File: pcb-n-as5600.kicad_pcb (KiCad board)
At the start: 2 copper layers, 31 x 31 mm, 31 parts, among them J1 Conn_01x04_Pin, J2 Conn_01x04_Pin, J3 Conn_01x04_Pin, J6 USB_C_Receptacle_USB2.0_14P, U1 AMS1117, U4 AS5600, U5 STM32F103C8Tx, Y2 8MHz

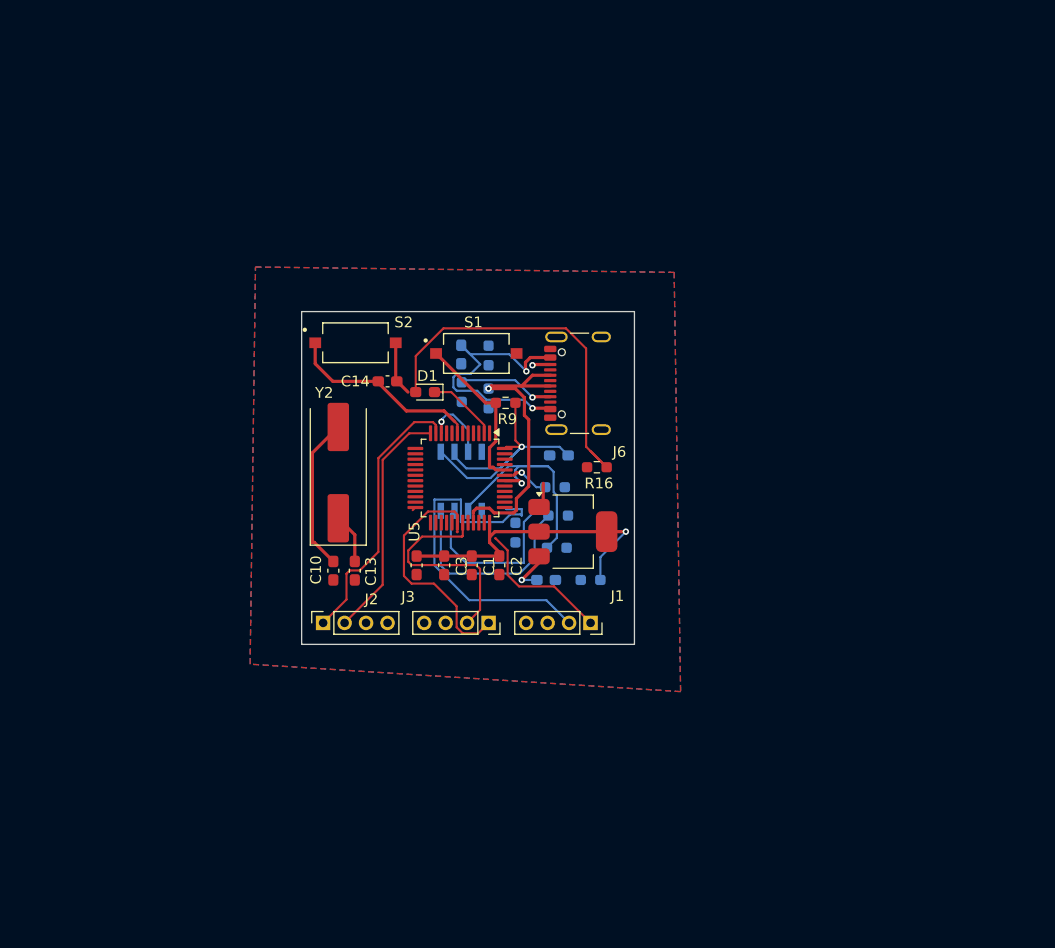
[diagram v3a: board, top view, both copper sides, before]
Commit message: addition of mount holes
rechecked voltage connections as well, and added
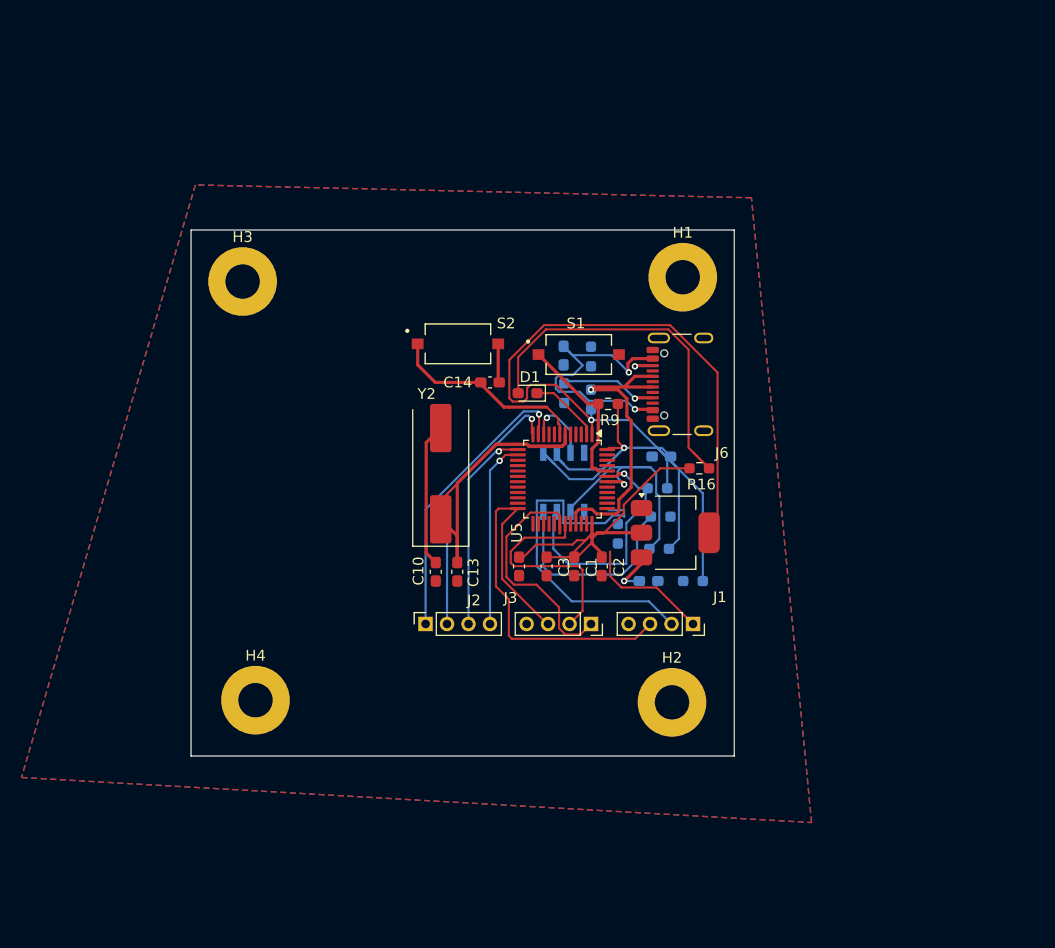
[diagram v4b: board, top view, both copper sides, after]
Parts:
- added H1: MountingHole, MountingHole:MountingHole_3.2mm_M3_Pad, F.Cu at (157.0, 53.8)
- added H2: MountingHole, MountingHole:MountingHole_3.2mm_M3_Pad, F.Cu at (156.0, 93.4)
- added H3: MountingHole, MountingHole:MountingHole_3.2mm_M3_Pad, F.Cu at (116.0, 54.2)
- added H4: MountingHole, MountingHole:MountingHole_3.2mm_M3_Pad, F.Cu at (117.2, 93.2)
- moved C11 9.54 mm to (141.8, 80.7)
- moved C2 9.54 mm to (149.5, 80.7)
- moved J1 9.54 mm to (158.0, 86.1)
- moved J3 9.54 mm to (148.5, 86.1)
- moved R11 9.54 mm to (146.0, 64.6)
- moved R13 9.54 mm to (154.6, 73.5)
- moved R2 9.54 mm to (148.5, 65.2)
- moved R3 9.54 mm to (151.0, 77.7)
- moved R4 9.54 mm to (158.0, 82.1)
- moved R7 9.54 mm to (154.8, 79.1)
- moved R8 9.54 mm to (148.5, 61.2)
- moved U1 9.54 mm to (156.3, 77.6)
- moved Y2 9.54 mm to (134.5, 72.1)
- moved C10 9.54 mm to (134.0, 81.2)
- moved C13 9.54 mm to (136.0, 81.2)
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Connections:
- J1 pad 3: /3.3V -> +3.3V
- J3 pad 3: /3.3V -> +3.3V
- R13 pad 1: /3.3V -> +3.3V
- R16 pad 2: /3.3V -> +3.3V
- R2 pad 1: /3.3V -> +3.3V
- R7 pad 1: /3.3V -> +3.3V
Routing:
- net +3.3V: track 58.3 -> 201.3 mm
- net /OSC_OUT: track 4.66 -> 41.2 mm
- net dum3: track 0.00 -> 19.3 mm, vias 0 -> 1
- net dum4: track 0.00 -> 17.5 mm, vias 0 -> 1
- net dum2: track 22.1 -> 24.6 mm, vias 0 -> 1
- net Net-(U1-ADJ): track 2.36 -> 0.55 mm
- net SWDIO: track 13.5 -> 11.9 mm
- net GND: track 5.07 -> 3.46 mm
- net dum1: track 25.7 -> 27.1 mm, vias 0 -> 1
- net /OSC_IN: track 14.4 -> 13.5 mm
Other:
- board size 31 x 31 mm -> 50.6 x 49 mm

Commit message: final pcb with proper connections
removed UART due to lack of use, connections are correct, slight silk screen issue, final draft
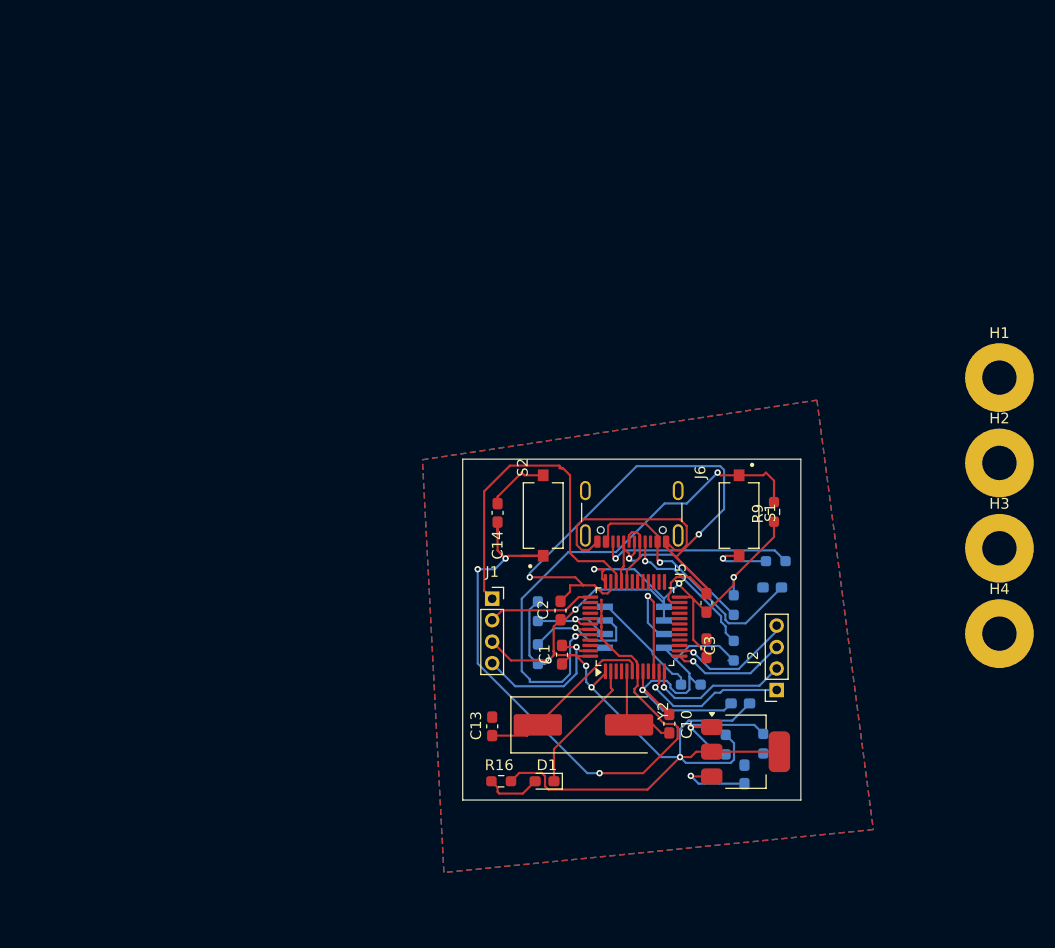
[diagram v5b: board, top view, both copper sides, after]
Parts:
- removed J3: Conn_01x04_Pin, Connector_PinSocket_2.00mm:PinSocket_1x04_P2.00mm_Vertical
- moved H3 74.8 mm to (186.5, 79.0)
- moved H4 69.6 mm to (186.5, 87.0)
- moved H2 37.8 mm to (186.5, 71.1)
- moved D1 36.2 mm to (144.1, 100.8)
- moved R16 34.5 mm to (140.1, 100.8), turned to 0 degrees
- moved J2 33.3 mm to (165.8, 92.2), turned to 180 degrees
- moved H1 30.9 mm to (186.5, 63.1)
- moved C8 29.1 mm to (165.3, 82.7), turned to 0 degrees
- moved R11 28.7 mm to (161.8, 88.6)
- moved Y2 26.9 mm to (147.8, 95.5), turned to 0 degrees
- moved C10 26.0 mm to (155.8, 95.4), turned to -90 degrees
- moved R8 25.7 mm to (165.7, 80.2), turned to 0 degrees
- moved C7 24.1 mm to (162.4, 93.5)
- moved R3 23.8 mm to (164.5, 97.2)
- moved R2 23.3 mm to (161.8, 84.3), turned to -90 degrees
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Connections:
- U5 pad 30: /TX -> unconnected-(U5-PA9-Pad30)
- U5 pad 31: /RX -> unconnected-(U5-PA10-Pad31)
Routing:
- net GND: track 3.46 -> 136.9 mm, vias 0 -> 5
- net +3.3V: track 201.3 -> 134.7 mm, vias 2 -> 8
- net NRST: track 18.7 -> 63.7 mm, vias 0 -> 3
- net BOOTO: track 14.4 -> 48.2 mm, vias 0 -> 2
- net Net-(D1-A): track 35.1 -> 5.28 mm
- net /OSC_OUT: track 41.2 -> 16.8 mm
- net SCLK: track 33.7 -> 10.0 mm
- net /TX: track 22.2 -> 0.00 mm
- net SWDIO: track 11.9 -> 33.0 mm
- net /RX: track 20.4 -> 0.00 mm
- net Net-(J6-CC2): track 1.69 -> 18.2 mm
- net SDA: track 24.1 -> 8.47 mm
- net Net-(U1-ADJ): track 0.55 -> 13.5 mm, vias 0 -> 1
- net dum1: track 27.1 -> 14.8 mm
- net dum2: track 24.6 -> 13.6 mm
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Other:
- board size 50.6 x 49 mm -> 31.5 x 31.8 mm

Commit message: final with mounting
changed shape of PCB to accomadate mounting holes
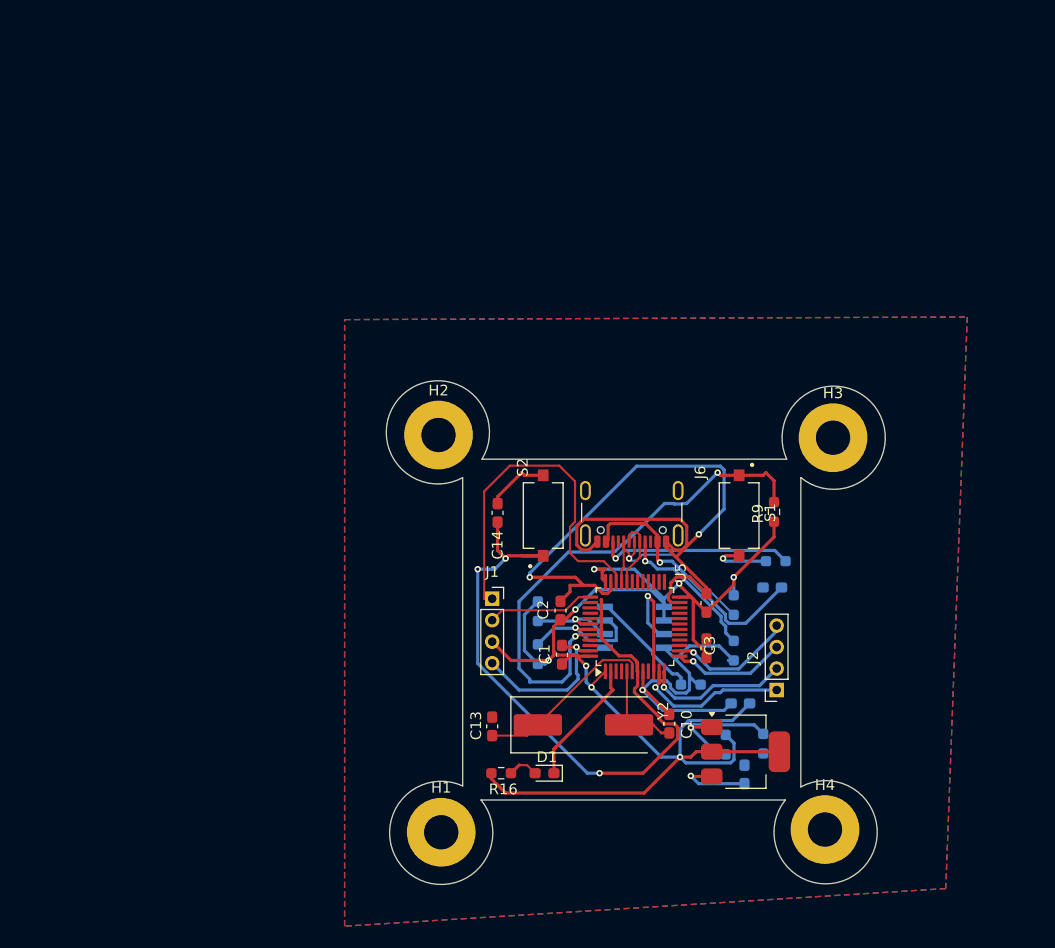
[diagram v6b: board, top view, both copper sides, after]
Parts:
- moved H1 67.1 mm to (134.5, 105.5)
- moved H2 52.3 mm to (134.2, 68.5)
- moved H4 24.4 mm to (170.2, 105.2)
- moved H3 18.6 mm to (171.0, 68.8)
- moved D1 0.75 mm to (144.1, 100.0)
- moved R16 0.75 mm to (140.1, 100.0), turned to 180 degrees
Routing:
- net Net-(D1-A): track 5.28 -> 2.89 mm
- net +3.3V: track 134.7 -> 136.6 mm
- net GND: track 136.9 -> 137.7 mm
- net SWDIO: track 33.0 -> 33.6 mm
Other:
- board size 31.5 x 31.8 mm -> 46.5 x 46.9 mm

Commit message: final changes
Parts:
- moved R2 1.18 mm to (161.8, 83.2)
- moved S2 0.90 mm to (143.2, 76.5)
- moved C14 0.75 mm to (139.0, 75.8)
- moved C4 0.37 mm to (163.0, 100.4)
- moved C10 0.25 mm to (155.8, 95.6)
- moved H2 0.25 mm to (134.2, 68.2)
- moved R1 0.25 mm to (157.8, 91.5)
- turned C3 to -90 degrees
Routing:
- net GND: track 137.7 -> 120.5 mm, vias 5 -> 7
- net NRST: track 63.7 -> 50.1 mm, vias 3 -> 2
- net /OSC_IN: track 9.13 -> 18.3 mm, vias 0 -> 2
- net SCL: track 12.4 -> 17.9 mm
- net SWDIO: track 33.6 -> 36.8 mm
- net dum2: track 13.6 -> 14.8 mm
- net Net-(J6-CC1): track 13.8 -> 14.7 mm
- net Net-(U4-DIR): track 10.6 -> 11.4 mm
- net Net-(C8-Pad2): track 24.8 -> 24.1 mm
- net dum4: track 11.7 -> 12.4 mm
- net +3.3V: track 136.6 -> 137.3 mm
- net dum3: track 10.7 -> 11.3 mm
- net +5V: track 7.27 -> 7.79 mm
- net MCU_D+: track 19.8 -> 19.3 mm

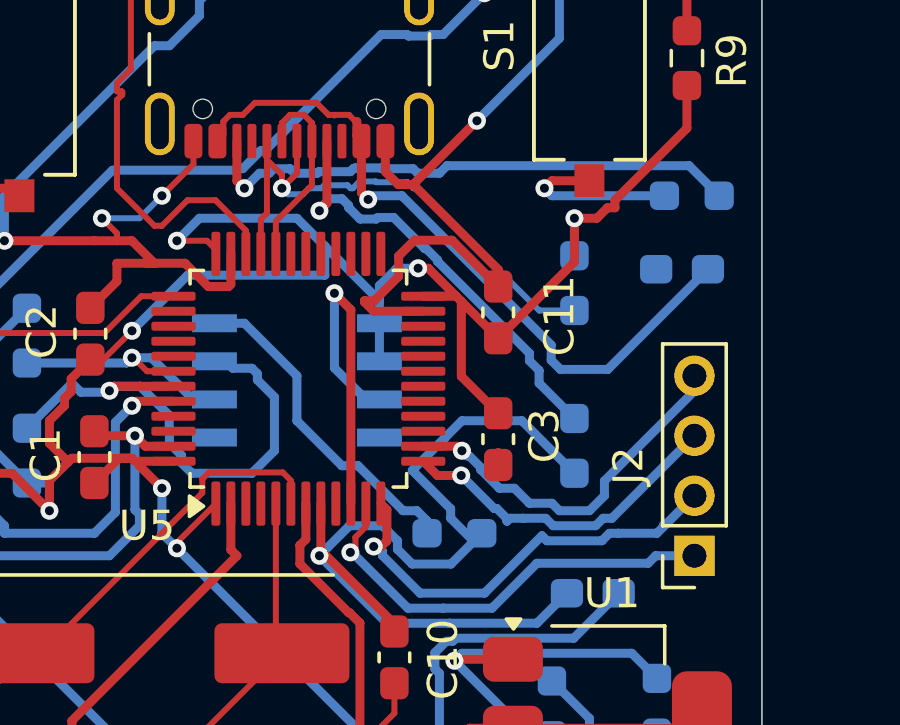
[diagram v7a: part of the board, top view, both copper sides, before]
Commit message: changed switch and updated BOM
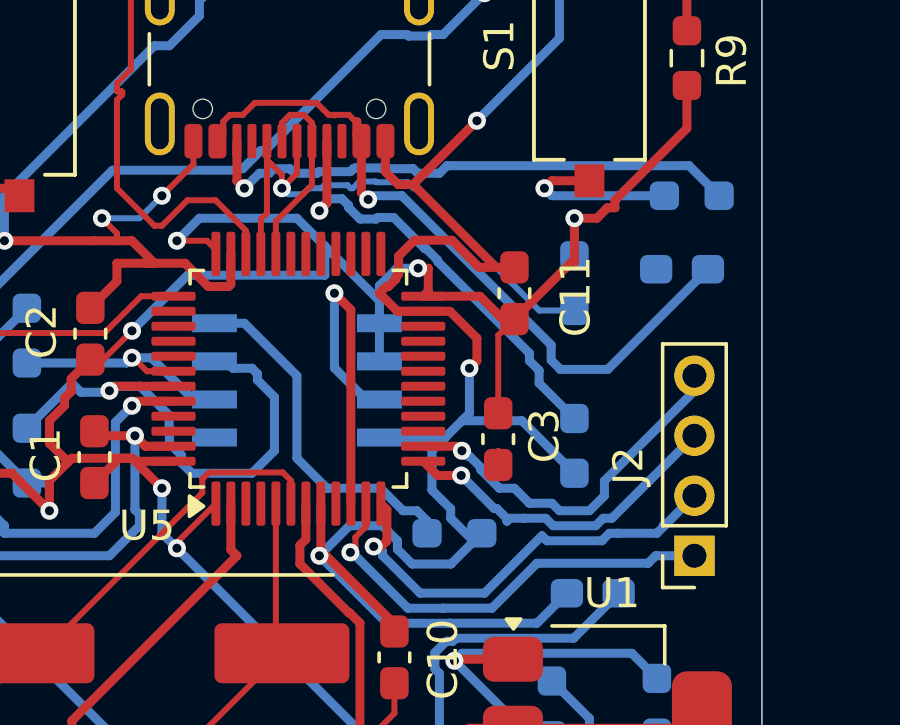
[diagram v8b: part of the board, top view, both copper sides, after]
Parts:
- moved C11 0.84 mm to (159.8, 83.5)
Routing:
- net GND: track 120.5 -> 125.5 mm, vias 7 -> 8
- net +3.3V: track 137.3 -> 135.5 mm
- net Net-(U4-DIR): track 11.4 -> 12.1 mm
